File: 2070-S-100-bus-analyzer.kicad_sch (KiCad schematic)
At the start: 84 parts, among them J10 Conn_02x13_Odd_Even, J11 Conn_02x13_Odd_Even, J12 USB4105-GF-A, J13 Conn_01x01, J14 Conn_01x01, J15 Conn_01x02, J16 Conn_01x02, J17 Conn_01x02, J18 Conn_01x02, J19 Conn_01x02, J2 Conn_02x13_Odd_Even, J3 Conn_02x13_Odd_Even, J4 Conn_02x13_Odd_Even, J5 Conn_02x13_Odd_Even, J6 Conn_02x13_Odd_Even, J7 Conn_02x13_Odd_Even, J8 Conn_02x13_Odd_Even, J9 Conn_02x13_Odd_Even, SW1 SW_MEC_5E, U1 74LVCH245APW,118, U10 74LVCH245APW,118, U11 74LVCH245APW,118, U12 74LVCH245APW,118, U13 74LVCH245APW,118, U14 74LVCH245APW,118, U15 74LVCH245APW,118, U16 AP63300, U17 LM7805_TO220, U2 74LVCH245APW,118, U3 74LVCH245APW,118, U4 74LVCH245APW,118, U5 74LVCH245APW,118, U6 74LVCH245APW,118, U7 74LVCH245APW,118, U8 74LVCH245APW,118, U9 74LVCH245APW,118

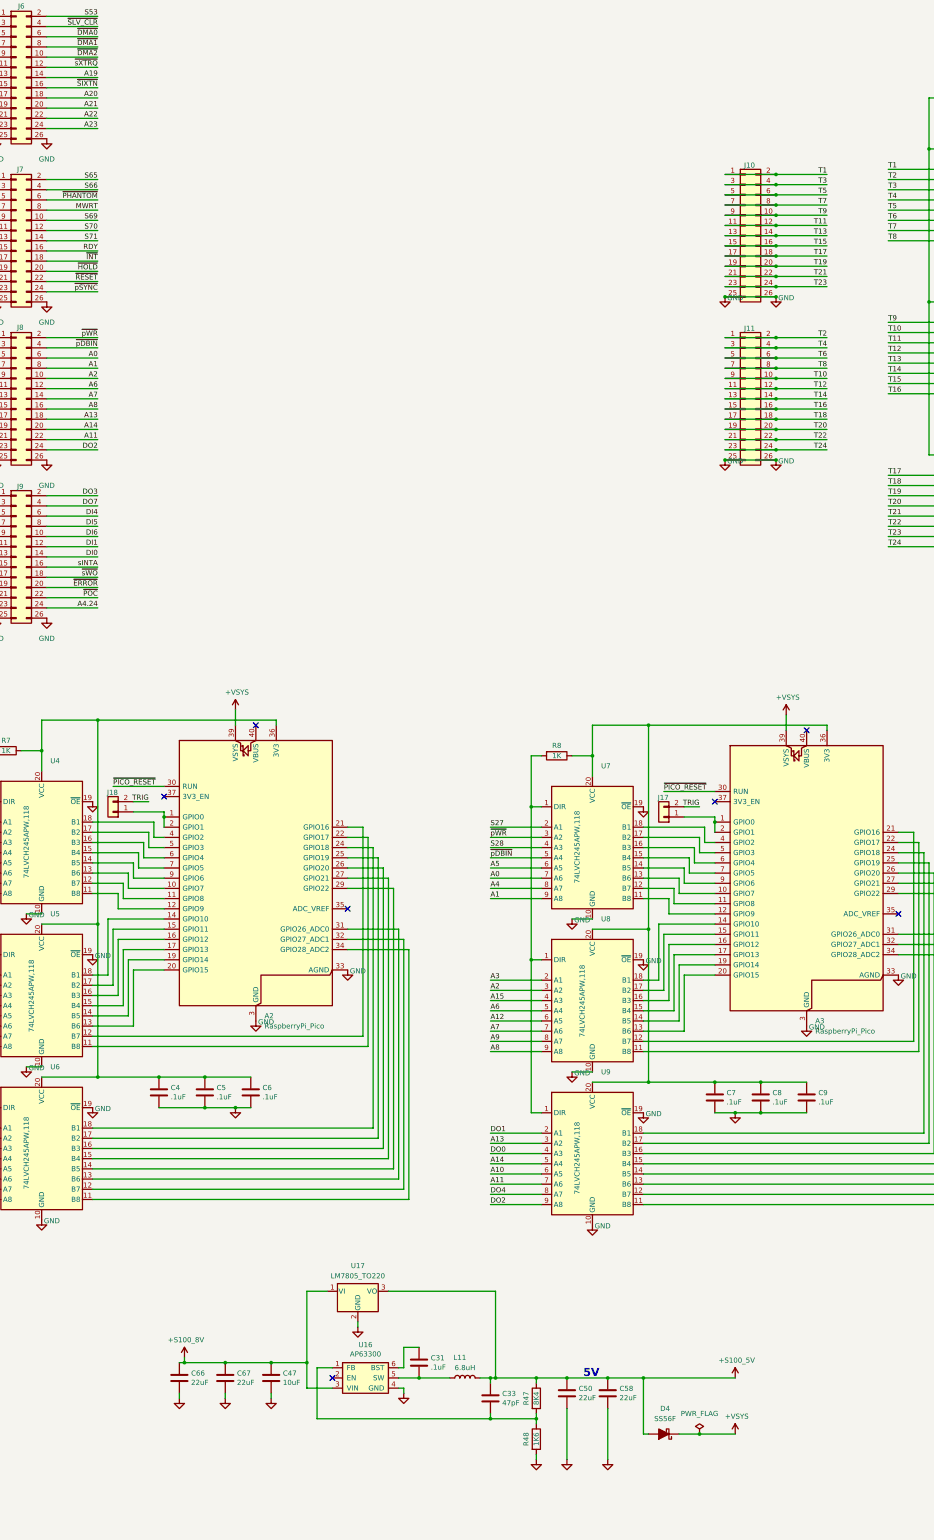
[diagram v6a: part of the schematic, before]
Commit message: DRC fixes Clean up power supplies
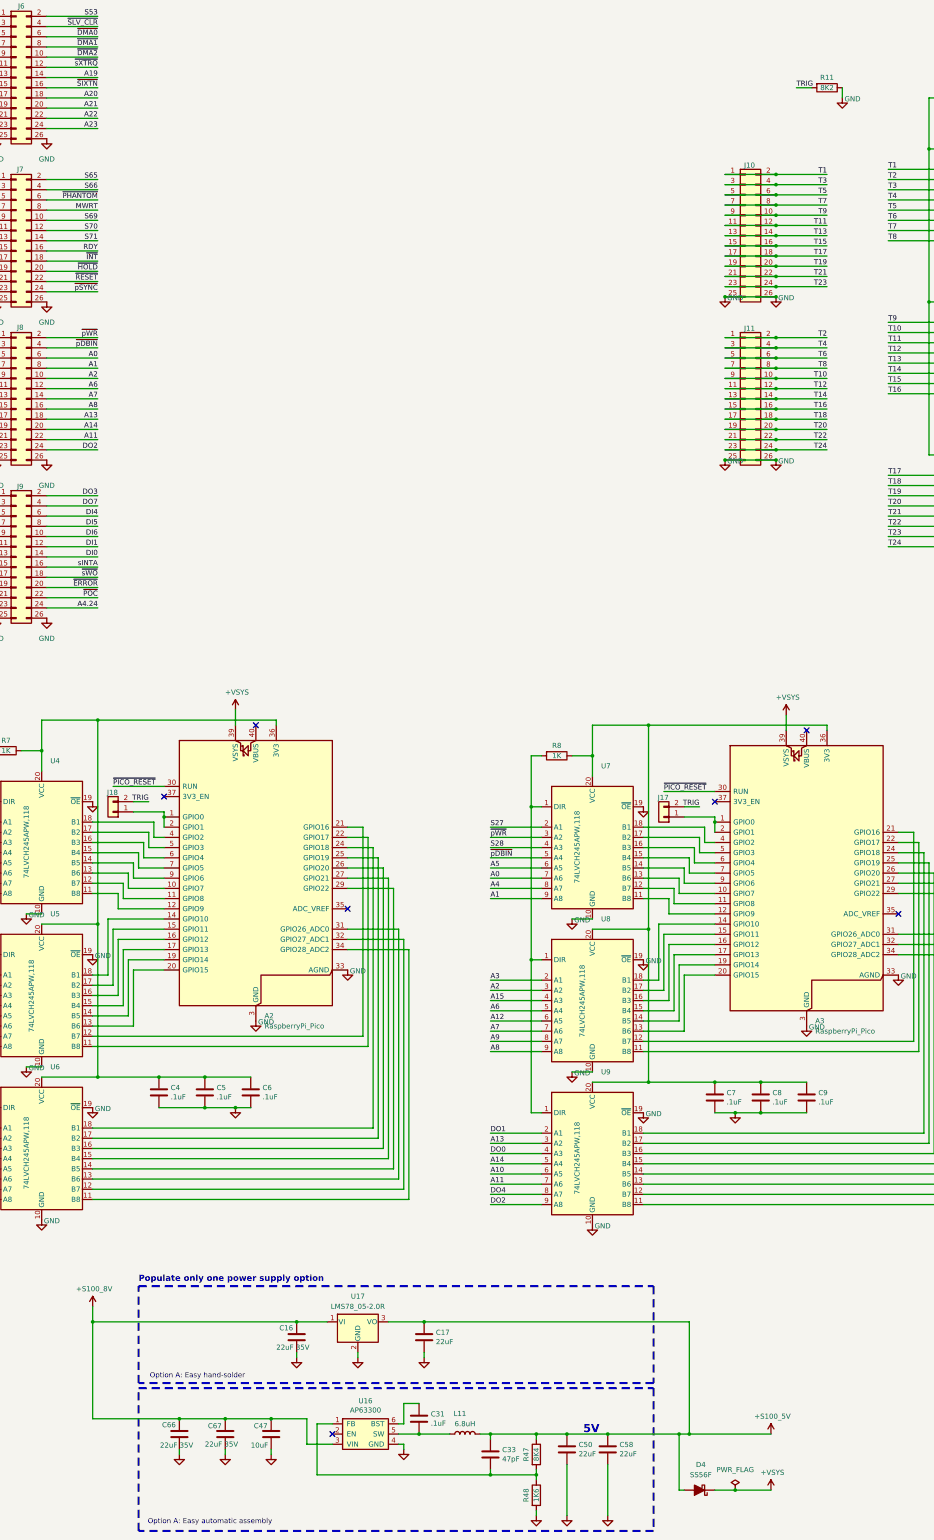
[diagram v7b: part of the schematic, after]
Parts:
- added C16: 22uF 35V, Capacitor_SMD:C_0805_2012Metric_Pad1.18x1.45mm_HandSolder, symbol Device:C
- added C17: 22uF, Capacitor_SMD:C_0805_2012Metric_Pad1.18x1.45mm_HandSolder, symbol Device:C
- added R11: 8K2, Resistor_SMD:R_0603_1608Metric_Pad0.98x0.95mm_HandSolder, symbol Device:R
- C66, C67: value 22uF -> 22uF 35V; Digi-Key_PN 490-14661-1-ND -> 445-14428-1-ND
- D4, D5: footprint Diode_SMD:D_SMB_Handsoldering -> Diode_SMD:D_SMB
- U17: value LM7805_TO220 -> LMS78_05-2.0R
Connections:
- net +S100_5V: now also C17.1
- net +S100_8V: now also C16.1
- net GND: now also C16.2, C17.2, R11.1
- net TRIG: now also R11.2
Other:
- note added: "Option A: Easy automatic assembly"
- note added: "Option A: Easy hand-solder"
- note added: "Populate only one power supply option"
- moved on the sheet: C31, C33, C47, C50, C58, C66, C67, D4, L11, R47, R48, U16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

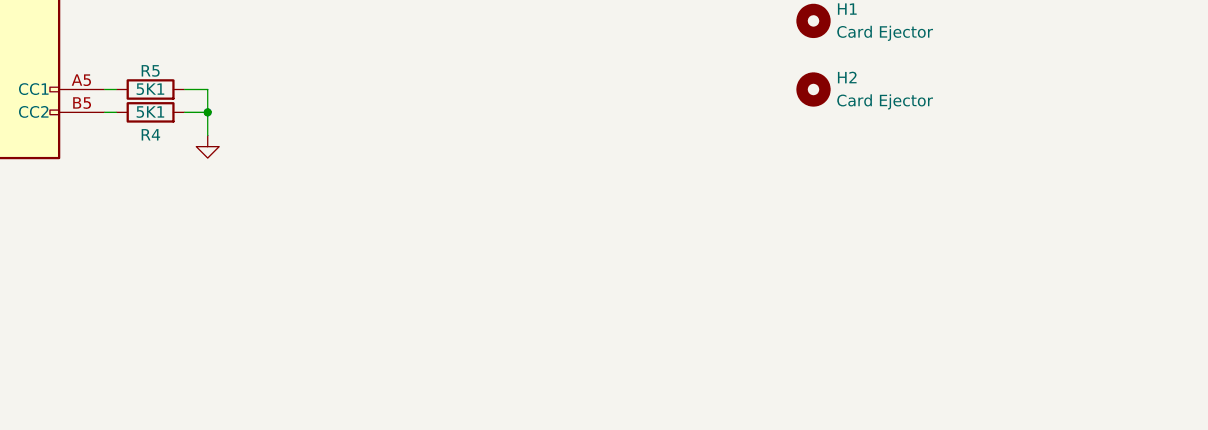
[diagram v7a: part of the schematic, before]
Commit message: Add title block
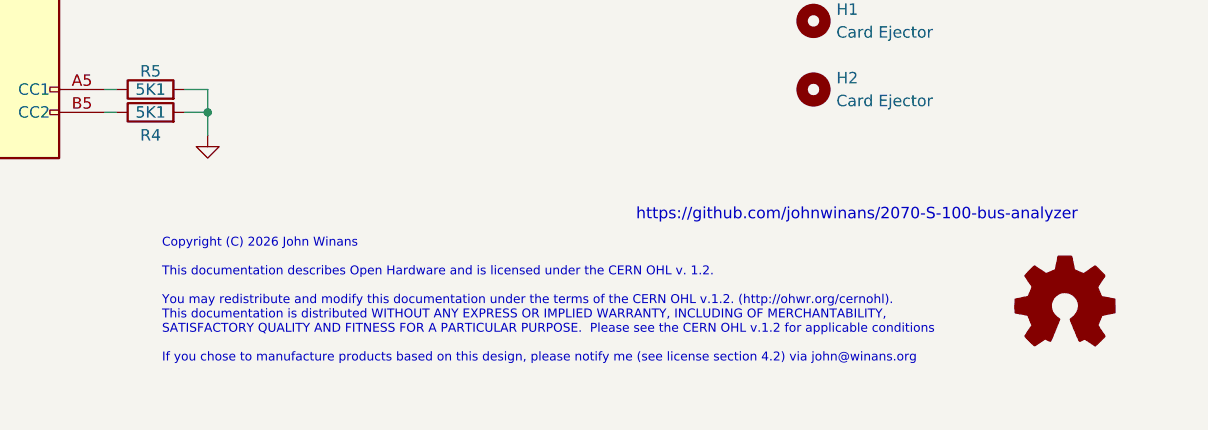
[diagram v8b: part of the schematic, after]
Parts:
- added LOGO1: OSHW_Logo, Symbol:OSHW-Logo_11.4x12mm_SilkScreen, symbol Graphic:Logo_Open_Hardware_Small
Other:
- note added: "Copyright (C) 2026 John Winans This documentation describes Open Hardware and is licensed under the CERN OHL v. 1.2. You may redistribute and modify this documentation under the terms of the CERN OHL v.1.2. (http://ohwr.org/cernohl). This documentation is distributed WITHOUT ANY EXPRESS OR IMPLIED WARRANTY, INCLUDING OF MERCHANTABILITY, SATISFACTORY QUALITY AND FITNESS FOR A PARTICULAR PURPOSE. P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"
- note added: "https://github.com/johnwinans/2070-S-100-bus-analyzer"
- title: (none) -> S-100 Bus Analyzer
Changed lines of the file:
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@@
 	(generator_version "9.0")
 	(paper "A2")
+	(title_block
+		(title "S-100 Bus Analyzer")
+		(date "2026-03-27")
+		(rev "Rev 1.0")
+	)
 	(rectangle
 		(start 240.03 335.28)
@@
 		)
 	)
+	(text "https://github.com/johnwinans/2070-S-100-bus-analyzer"
+		(exclude_from_sim no)
+		(at 552.196 374.65 0)
+		(effects
+			(font
+				(size 1.27 1.27)
+			)
+		)
+	)
 	(text "Option A: Easy hand-solder"
 		(exclude_from_sim no)
@@
 		)
 	)
+	(text "Copyright (C) 2026 John Winans\n\nThis documentation describes Open Hardware and is licensed under the CERN OHL v. 1.2.\n\nYou may redistribute and modify this documentation under the terms of the CERN OHL v.1.2. (http://ohwr.org/cernohl). \nThis documentation is distributed WITHOUT ANY EXPRESS OR IMPLIED WARRANTY, INCLUDING OF MERCHANTABILITY, \nSATISFACTORY QUALITY AND FITNESS FOR A PARTICULAR PURPOSE.  Please see the CERN OHL v.1.2 for applicable conditions\n\nIf you chose to manufacture products based on this design, please notify me (see license section 4.2) via john@winans.org\n"
+		(exclude_from_sim no)
+		(at 474.98 391.16 0)
+		(effects
+			(font
+				(size 0.9906 0.9906)
+			)
+			(justify left bottom)
+		)
+	)
 	(text "5V"
 		(exclude_from_sim no)
@@
 					(unit 1)
 				)
+			)
+		)
+	)
+	(symbol
+		(lib_id "Graphic:Logo_Open_Hardware_Small")
+		(at 575.31 384.81 0)
+		(unit 1)
+		(exclude_from_sim no)
+		(in_bom yes)
+		(on_board yes)
+		(dnp no)
+		(property "Reference" "LOGO1"
+			(at 575.31 377.825 0)
+			(effects
+				(font
+					(size 1.27 1.27)
+				)
+				(hide yes)
+			)
+		)
+		(property "Value" "OSHW_Logo"
+			(at 575.31 390.525 0)
+			(effects
+				(font
+					(size 1.27 1.27)
+				)
+				(hide yes)
+			)
+		)
+		(property "Footprint" "Symbol:OSHW-Logo_11.4x12mm_SilkScreen"
+			(at 575.31 384.81 0)
+			(effects
+				(font
+					(size 1.27 1.27)
+				)
+				(hide yes)
+			)
+		)
+		(property "Datasheet" ""
+			(at 575.31 384.81 0)
+			(effects
+				(font
+					(size 1.27 1.27)
+				)
+				(hide yes)
+			)
+		)
+		(property "Description" ""
+			(at 575.31 384.81 0)
+			(effects
+				(font
+					(size 1.27 1.27)
+				)
+			)
+		)
+		(instances
+			(project "2070-S-100-bus-analyzer"
+				(path "/e6802e0a-d78e-48fb-9644-7dc83bb4bf35"
+					(reference "LOGO1")
+					(unit 1)
+				)
